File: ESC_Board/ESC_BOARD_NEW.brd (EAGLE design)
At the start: 162.6 x 175.5 mm, 187 parts, among them J3 AVR_SPI_PROG_3X2NS, U2 ATMEGA328P_TQFP, U4 PCA9685

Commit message: More layout stuff
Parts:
- removed C76, C77: 0.1uF, rcl:C0603
- removed LED7, LED8: WS2812B5050, microbuilder:WS2812B
- moved P8 345.7 mm to (113.8, -53.8)
- moved P4 344.9 mm to (127.0, -53.8)
- moved P7 344.4 mm to (117.1, -53.8)
- moved P6 343.0 mm to (120.4, -53.8)
- moved P5 341.7 mm to (123.7, -53.8)
- moved P3 339.0 mm to (130.3, -53.8)
- moved P2 337.7 mm to (133.6, -53.8)
- moved P1 336.4 mm to (136.9, -53.8)
- moved C15 332.4 mm to (131.8, -18.8)
- moved U$16 330.9 mm to (149.1, -27.7)
- moved J3 330.3 mm to (149.1, -13.5), turned to 90 degrees
- moved C14 329.2 mm to (131.8, -21.8)
- moved C17 328.4 mm to (104.9, -30.2), turned to 270 degrees
- moved C13 326.2 mm to (131.8, -24.9)
- moved C12 323.2 mm to (131.8, -27.9)
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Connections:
- removed net OUT7: LED7.2-DOUT, LED8.4-DIN
- net +5V: no longer C76.1, C77.1, LED7.1-VDD, LED8.1-VDD
- net GND: no longer C76.2, C77.2, LED7.3-GND, LED8.3-GND
- net OUT3: no longer LED8.2-DOUT
- net OUT6: no longer LED7.4-DIN
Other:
- board size 162.6 x 175.5 mm -> 162.6 x 167.4 mm

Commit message: Layout work
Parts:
- removed C53, C54, C55, C57, C58, C59, C60, C61, C7, C8, C9: 0.1uF, SparkFun-Capacitors:0603
- removed R22, R23, R24, R25, R28, R29, R30, R31, R32, R33, R34, R35, R36, R37, R4, R5, R6, R7, R8, R9: (no value), rcl:R0603
- removed U$14: MCP3008, MCP3008:MCP3008
- added ESC7_CON1, ESC7_CON3, ESC7_CON4: 3PINCONNECTOR, afro_20A_esc:3PINCONNECTOR
- added F1, F10, F11, F2, F3, F4, F5, F6, F7, F8, F9: 10A, PowerComponents:PTC-2920
- added J1, J2, J4, J5: (no value), SparkFun-Connectors:1X02
- moved C73 191.3 mm to (-47.0, 113.5)
- moved LED3 189.7 mm to (-115.6, 115.8)
- moved LED4 189.0 mm to (-38.1, 113.8)
- moved C72 188.2 mm to (-108.2, 114.3)
- moved LED2 187.4 mm to (-188.5, 112.3)
- moved C1 187.2 mm to (-139.2, -38.4)
- moved C10 187.2 mm to (-141.0, -50.5)
- moved C11 187.2 mm to (-66.8, -13.7)
- moved C16 187.2 mm to (-82.3, -21.6)
- moved C17 187.2 mm to (-82.3, -28.7)
- moved C2 187.2 mm to (-141.5, -38.4)
- moved C3 187.2 mm to (-146.1, -38.4)
- moved C56 187.2 mm to (-182.6, -38.4)
- moved C62 187.2 mm to (-150.6, -38.4)
- moved C65 187.2 mm to (-166.6, -38.4)
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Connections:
- removed net ANALOG_6: U$14.CH6
- removed net N$52: U$14.CH7
- removed net PWM12: U4.19
- removed net PWM13: P13.1, U4.20
- removed net PWM14: P14.1, U4.21
- removed net TEMP1: C57.1, R28.1, R29.2, U$4.CH0
- removed net TEMP10: C55.1, R24.1, R25.2, U$14.CH2
- removed net TEMP2: C58.1, R30.1, R31.2, U$4.CH2
- removed net TEMP3: C59.1, R32.1, R33.2, U$4.CH4
- removed net TEMP4: C60.1, R34.1, R35.2, U$4.CH6
- removed net TEMP5: C61.1, R36.1, R37.2, U$13.CH0
- removed net TEMP6: C7.1, R4.1, R5.2, U$13.CH2
- removed net TEMP7: C8.1, R6.1, R7.2, U$13.CH4
- removed net TEMP8: C9.1, R8.1, R9.2, U$13.CH6
- removed net TEMP9: C54.1, R22.1, R23.2, U$14.CH0
- new net E1: J5.2, U$13.CH4
- new net E2: J4.2, U$13.CH5
- new net E3: J1.2, U$13.CH6
- new net E4: J2.2, U$13.CH7
- new net LED1: ESC7_CON1.B, U4.19
- new net LED2: ESC7_CON3.B, P13.1, U4.20
- new net N$51: F6.1, U$7.IP1+, U$7.IP2+
- new net N$53: F1.1, U$1.IP1+, U$1.IP2+
- new net N$54: F2.1, U$2.IP1+, U$2.IP2+
- new net N$55: F3.1, U$3.IP1+, U$3.IP2+
- new net N$56: F4.1, U$5.IP1+, U$5.IP2+
- new net N$57: F5.1, U$6.IP1+, U$6.IP2+
- new net N$58: F7.1, U$8.IP1+, U$8.IP2+
- new net N$60: F8.1, U$9.IP1+, U$9.IP2+
- new net N$61: F9.1, U$10.IP1+, U$10.IP2+
- new net N$62: F10.1, U$11.IP1+, U$11.IP2+
- new net N$63: F11.1, U$12.IP1+, U$12.IP2+
- new net PIEZO: ESC7_CON4.B, P14.1, U4.21
- net +12V: now also ESC7_CON1.C, ESC7_CON3.C, ESC7_CON4.C, F1.2, F10.2, F11.2, F2.2, F3.2, F4.2, F5.2, F6.2, F7.2, F8.2, F9.2; no longer U$1.IP1+, U$1.IP2+, U$10.IP1+, U$10.IP2+, U$11.IP1+, U$11.IP2+, U$12.IP1+, U$12.IP2+, U$2.IP1+, U$2.IP2+, U$3.IP1+, U$3.IP2+, U$5.IP1+, U$5.IP2+, U$6.IP1+, U$6.IP2+, U$7.IP1+, U$7.IP2+, U$8.IP1+, U$8.IP2+, U$9.IP1+, U$9.IP2+
- net +5V: no longer C53.1, R22.2, R24.2, R28.2, R30.2, R32.2, R34.2, R36.2, R4.2, R6.2, R8.2, U$14.VDD, U$14.VREF
- net CS: no longer U$14.CS/SHDN
- net CUR1: now also U$4.CH0; no longer U$4.CH1
- net CUR10: now also U$13.CH1; no longer U$14.CH3
- net CUR11: now also U$13.CH2; no longer U$14.CH5
- net CUR2: now also U$4.CH1; no longer U$4.CH3
- net CUR3: now also U$4.CH2; no longer U$4.CH5
- net CUR4: now also U$4.CH3; no longer U$4.CH7
- net CUR5: now also U$4.CH4; no longer U$13.CH1
- net CUR6: now also U$4.CH5; no longer U$13.CH3
- net CUR7: now also U$4.CH6; no longer U$13.CH5
- net CUR8: now also U$4.CH7; no longer U$13.CH7
- net CUR9: now also U$13.CH0; no longer U$14.CH1
- net GND: now also ESC7_CON1.A, ESC7_CON3.A, ESC7_CON4.A, J1.1, J2.1, J4.1, J5.1; no longer C53.2, C54.2, C55.2, C57.2, C58.2, C59.2, C60.2, C61.2, C7.2, C8.2, C9.2, R23.1, R25.1, R29.1, R31.1, R33.1, R35.1, R37.1, R5.1, R7.1, R9.1, U$14.AGND, U$14.DGND
- net MISO: no longer U$14.DOUT
- net MOSI: no longer U$14.DIN
- net SCK: no longer U$14.CLK
- net TEMP11: now also U$13.CH3; no longer U$14.CH4
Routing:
- removed copper zone on layer 1, net GND
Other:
- board size 162.6 x 167.4 mm -> 127 x 177.8 mm

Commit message: Initial layout
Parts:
- moved ESC7_CON4 575.4 mm to (95.2, 173.2), turned to 180 degrees
- moved J2 553.8 mm to (121.4, 48.3)
- moved ESC7_CON3 538.2 mm to (95.2, 155.4), turned to 180 degrees
- moved J1 535.1 mm to (121.4, 44.2)
- moved J5 529.7 mm to (121.4, 56.4)
- moved ESC7_CON1 524.3 mm to (95.2, 164.3), turned to 180 degrees
- moved J4 511.4 mm to (121.4, 52.3)
- moved F11 368.4 mm to (64.3, 4.32), turned to 180 degrees
- moved F10 340.6 mm to (43.4, 4.57), flipped to the bottom
- moved F7 326.1 mm to (43.9, 39.9), flipped to the bottom
- moved F5 324.9 mm to (44.5, 75.2), flipped to the bottom
- moved F8 324.6 mm to (22.4, 39.9), flipped to the bottom, turned to 180 degrees
- moved F6 323.4 mm to (23.1, 75.2), flipped to the bottom, turned to 180 degrees
- moved C69 320.2 mm to (109.5, 87.6), turned to 0 degrees
- moved C56 319.1 mm to (109.5, 90.2), turned to 180 degrees
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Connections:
- net LED1: now also P12.1

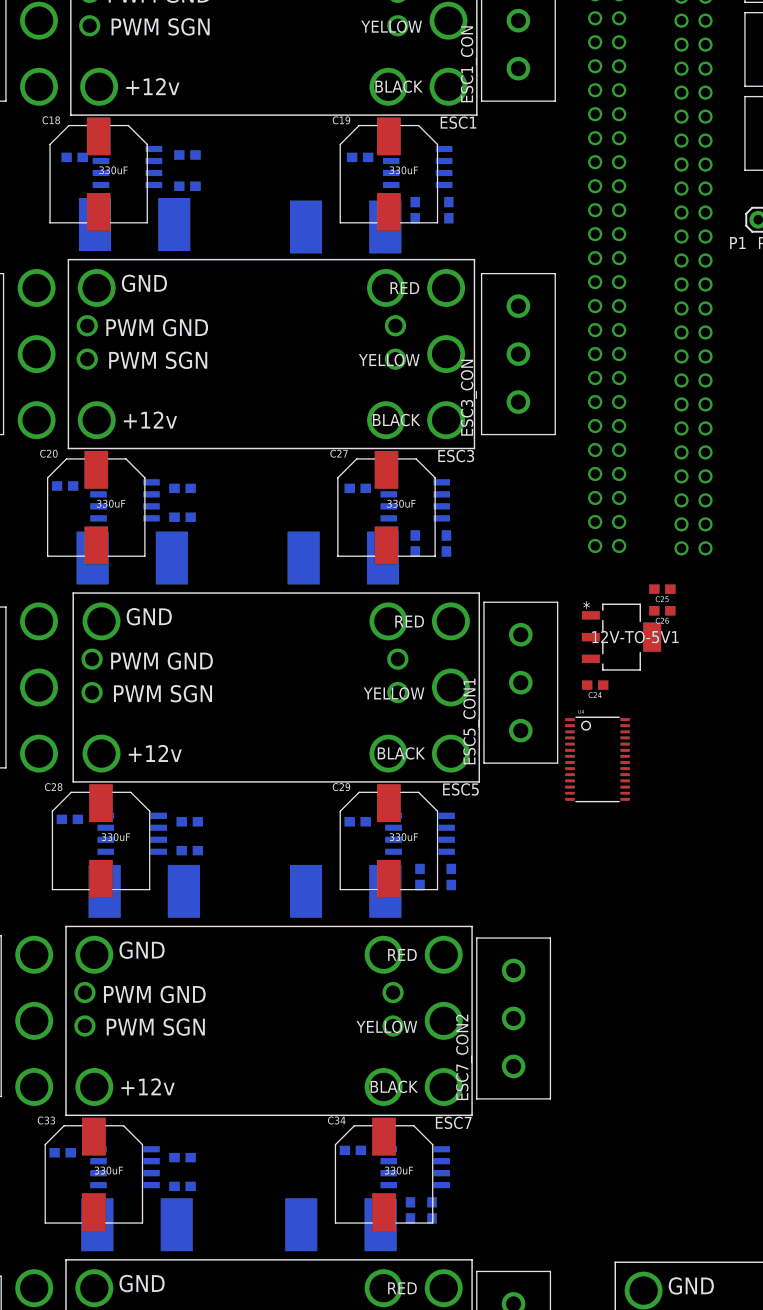
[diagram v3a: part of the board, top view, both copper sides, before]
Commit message: more board routing
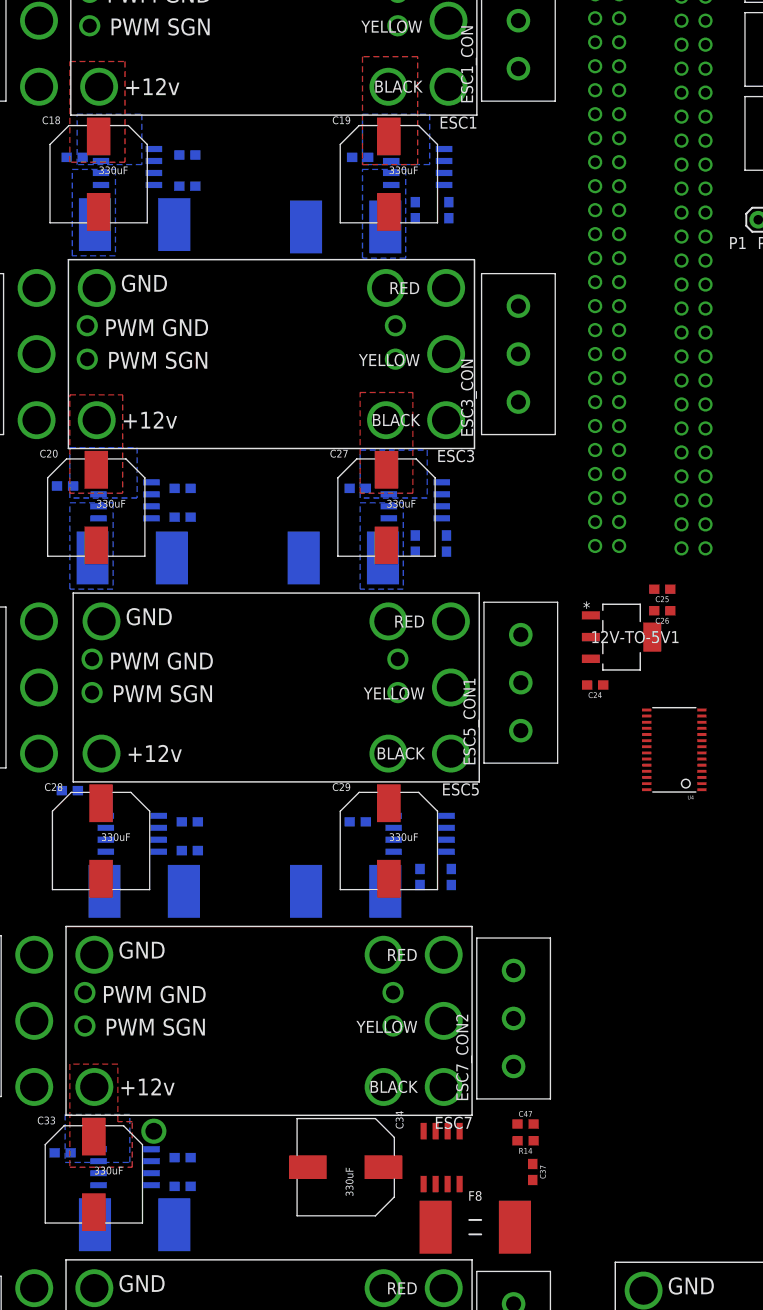
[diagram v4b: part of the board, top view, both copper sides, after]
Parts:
- moved F8 35.8 mm to (58.2, 39.6), flipped to the top, turned to 0 degrees
- moved F7 21.8 mm to (22.1, 39.9), turned to 180 degrees
- moved C37 19.2 mm to (64.3, 45.5), flipped to the top, turned to 270 degrees
- moved R14 14.2 mm to (63.5, 48.8), flipped to the top, turned to 180 degrees
- moved C47 13.5 mm to (63.5, 50.5), flipped to the top, turned to 0 degrees
- moved U4 8.19 mm to (79.2, 90.2), turned to 90 degrees
- moved C34 4.13 mm to (44.5, 46.0), turned to 270 degrees
- moved C31 3.05 mm to (15.2, 85.9)
- moved U$9 2.97 mm to (54.6, 47.0), flipped to the top, turned to 90 degrees
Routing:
- added copper zone on layer 1, net ESC1
- added copper zone on layer 16, net ESC1
- added copper zone on layer 1, net ESC2
- added copper zone on layer 16, net ESC2
- added copper zone on layer 1, net ESC3
- added copper zone on layer 16, net ESC3
- added copper zone on layer 1, net ESC4
- added copper zone on layer 16, net ESC4
- added copper zone on layer 1, net ESC7
- added copper zone on layer 16, net ESC7
- added copper zone on layer 16, net N$53
- added copper zone on layer 16, net N$54
- added copper zone on layer 16, net N$55
- added copper zone on layer 16, net N$56

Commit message: routing abomination in progress
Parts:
- moved C37 19.2 mm to (45.2, 47.8), flipped to the bottom, turned to 0 degrees
- moved R14 14.3 mm to (51.6, 40.9), flipped to the bottom, turned to 270 degrees
- moved F8 14.2 mm to (43.9, 39.9), flipped to the bottom
- moved C47 12.6 mm to (55.4, 40.9), flipped to the bottom, turned to 90 degrees
- moved C4 5.08 mm to (27.7, 154.9), turned to 0 degrees
- moved C44 4.83 mm to (27.9, 84.3), turned to 0 degrees
- moved C46 4.83 mm to (27.2, 48.8), turned to 0 degrees
- moved C48 4.83 mm to (26.9, 13.7), turned to 0 degrees
- moved C6 4.83 mm to (27.2, 119.6), turned to 0 degrees
- moved C34 4.13 mm to (48.5, 45.2), turned to 0 degrees
- moved C31 3.30 mm to (15.2, 82.5)
- moved U$9 3.07 mm to (51.8, 45.7), flipped to the bottom, turned to 180 degrees
- moved C56 2.54 mm to (109.5, 87.6)
- moved C69 2.54 mm to (109.5, 90.2)
- moved C16 1.80 mm to (94.5, 67.6), turned to 270 degrees
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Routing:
- net +5V: track 0.00 -> 48.9 mm
- net +12V: track 0.00 -> 17.8 mm
- net CUR1: track 0.00 -> 9.37 mm
- net CUR8: track 0.00 -> 9.22 mm
- net N$10: track 0.00 -> 8.45 mm
- net N$12: track 0.00 -> 8.45 mm
- net N$18: track 0.00 -> 8.41 mm
- net N$37: track 0.00 -> 8.30 mm
- net N$33: track 0.00 -> 8.30 mm
- net N$30: track 0.00 -> 8.30 mm
- net N$19: track 0.00 -> 8.20 mm
- net N$5: track 0.00 -> 8.20 mm
- net N$9: track 0.00 -> 8.20 mm
- net N$25: track 0.00 -> 8.20 mm
- net N$24: track 0.00 -> 8.20 mm
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- added copper zone on layer 16, net +12V
- added copper zone on layer 1, net ESC10
- added copper zone on layer 16, net ESC10
- added copper zone on layer 1, net ESC5
- added copper zone on layer 16, net ESC5
- added copper zone on layer 1, net ESC6
- added copper zone on layer 16, net ESC6
- added copper zone on layer 1, net ESC8
- added copper zone on layer 16, net ESC8
- added copper zone on layer 1, net ESC9
- added copper zone on layer 16, net ESC9
- added copper zone on layer 16, net N$51
- added copper zone on layer 16, net N$57
- added copper zone on layer 16, net N$58
- added copper zone on layer 16, net N$60
- added copper zone on layer 16, net N$61
- added copper zone on layer 16, net N$62
- added copper zone on layer 1, net RESET

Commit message: The fun continues
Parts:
- moved C12 24.3 mm to (99.3, 75.2), turned to 90 degrees
- moved C15 19.4 mm to (101.9, 75.2), turned to 90 degrees
- moved C11 3.25 mm to (111.8, 79.8)
- moved R10 3.25 mm to (111.8, 81.5)
- moved RESET 3.25 mm to (105.7, 80.5)
- moved C14 2.74 mm to (118.6, 69.6)
- moved C16 2.65 mm to (97.0, 68.3)
- moved C17 2.65 mm to (97.0, 64.8)
- moved Y2 2.65 mm to (100.8, 66.8)
- moved C13 2.59 mm to (118.6, 67.1)
- turned C51 to 180 degrees
- turned R38 to 0 degrees
- turned R39 to 0 degrees
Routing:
- net +5V: track 48.9 -> 72.2 mm
- net N$15: track 7.80 -> 15.0 mm
- net N$14: track 7.66 -> 14.8 mm
- net SCL: track 0.00 -> 3.32 mm
- net SDA: track 0.00 -> 3.32 mm
- added copper zone on layer 1, net +12V

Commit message: Santa is dead and this board killed him
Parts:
- moved U$16 127.1 mm to (91.4, 43.7), turned to 180 degrees
- moved ESC7_CON4 122.0 mm to (89.7, 51.3), turned to 270 degrees
- moved ESC7_CON1 115.2 mm to (72.9, 51.3), turned to 270 degrees
- moved ESC7_CON3 105.1 mm to (81.3, 51.3), turned to 270 degrees
- moved C51 78.3 mm to (83.6, 74.9), flipped to the bottom, turned to 90 degrees
- moved R20 77.1 mm to (81.0, 74.9), flipped to the bottom, turned to 90 degrees
- moved R21 75.5 mm to (79.0, 74.9), flipped to the bottom, turned to 90 degrees
- moved R19 74.6 mm to (77.0, 74.9), flipped to the bottom, turned to 270 degrees
- moved P4 63.6 mm to (82.5, 84.6)
- moved P3 62.4 mm to (85.6, 84.6), turned to 0 degrees
- moved P1 61.8 mm to (91.7, 84.6), turned to 0 degrees
- moved P2 61.8 mm to (88.6, 84.6), turned to 0 degrees
- moved P8 61.5 mm to (72.9, 64.5), turned to 180 degrees
- moved P9 57.5 mm to (75.9, 64.5), turned to 180 degrees
- moved P10 53.5 mm to (79.0, 64.5), turned to 180 degrees
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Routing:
- net PWM0: track 0.00 -> 22.0 mm
- net PWM1: track 0.00 -> 19.7 mm
- net PWM15: track 0.00 -> 19.5 mm
- net PWM2: track 0.00 -> 17.2 mm
- net PIEZO: track 0.00 -> 17.2 mm
- net +5V: track 72.2 -> 87.6 mm, vias 0 -> 4
- net LED2: track 0.00 -> 15.2 mm
- net PWM3: track 0.00 -> 14.3 mm
- net LED1: track 0.00 -> 12.8 mm
- net PWM4: track 0.00 -> 11.8 mm
- net PWM11: track 0.00 -> 10.7 mm
- net PWM5: track 0.00 -> 9.62 mm
- net PWM10: track 0.00 -> 8.47 mm
- net PWM6: track 0.00 -> 8.18 mm
- net PWM7: track 0.00 -> 7.80 mm
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
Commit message: How does that saying go? Trial by fire?
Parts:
- moved U$16 128.4 mm to (115.1, 169.9), turned to 270 degrees
- moved R38 110.2 mm to (106.4, 161.5)
- moved SV2 110.2 mm to (116.8, 162.6)
- moved R39 110.2 mm to (106.4, 163.6)
- moved J3 93.7 mm to (102.6, 138.4), turned to 180 degrees
- moved C16 80.8 mm to (85.6, 148.3)
- moved U2 80.8 mm to (99.1, 149.1)
- moved C13 80.8 mm to (107.2, 147.1)
- moved C17 80.8 mm to (85.6, 144.8)
- moved R10 80.8 mm to (100.3, 161.5)
- moved Y2 80.8 mm to (89.4, 146.8)
- moved C11 80.8 mm to (100.3, 159.8)
- moved C12 80.8 mm to (87.9, 155.2)
- moved C14 80.8 mm to (107.2, 149.6)
- moved C15 80.8 mm to (90.4, 155.2)
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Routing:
- net RESET: track 0.00 -> 21.2 mm, vias 0 -> 2
- net PIEZO: track 17.2 -> 37.9 mm
- net SCL: track 3.32 -> 22.0 mm, vias 0 -> 1
- net SDA: track 3.32 -> 21.6 mm, vias 0 -> 1
- net LED2: track 15.2 -> 30.4 mm
- net LED1: track 12.8 -> 27.7 mm
- net E4: track 0.00 -> 13.9 mm
- net E3: track 0.00 -> 12.4 mm
- net E2: track 0.00 -> 10.2 mm
- net MOSI: track 0.00 -> 8.44 mm
- net E1: track 0.00 -> 7.93 mm
- net MISO: track 0.00 -> 6.62 mm
- net SCL_BRICKS: track 6.32 -> 12.1 mm, vias 0 -> 1
- net SDA_BRICKS: track 5.96 -> 10.1 mm, vias 1 -> 0
